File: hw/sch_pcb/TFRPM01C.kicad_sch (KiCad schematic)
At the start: 22 parts, among them J1 HEADER_1x03, J2 SM04B-GHS-TB, J3 SM04B-GHS-TB, M2 M3, U1 PCF8583, U2 SN74LVC1G14-Q1, U3 MIC5504-3.3YM5

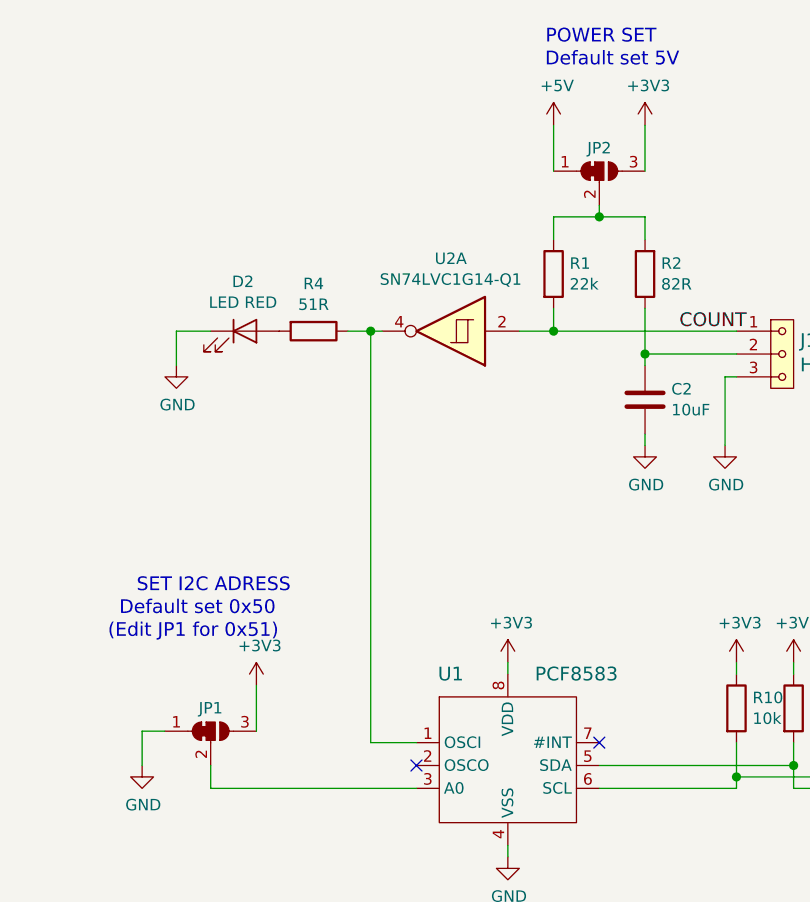
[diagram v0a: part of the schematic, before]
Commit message: update to newest kicad version, set schematic tempate, clean dps
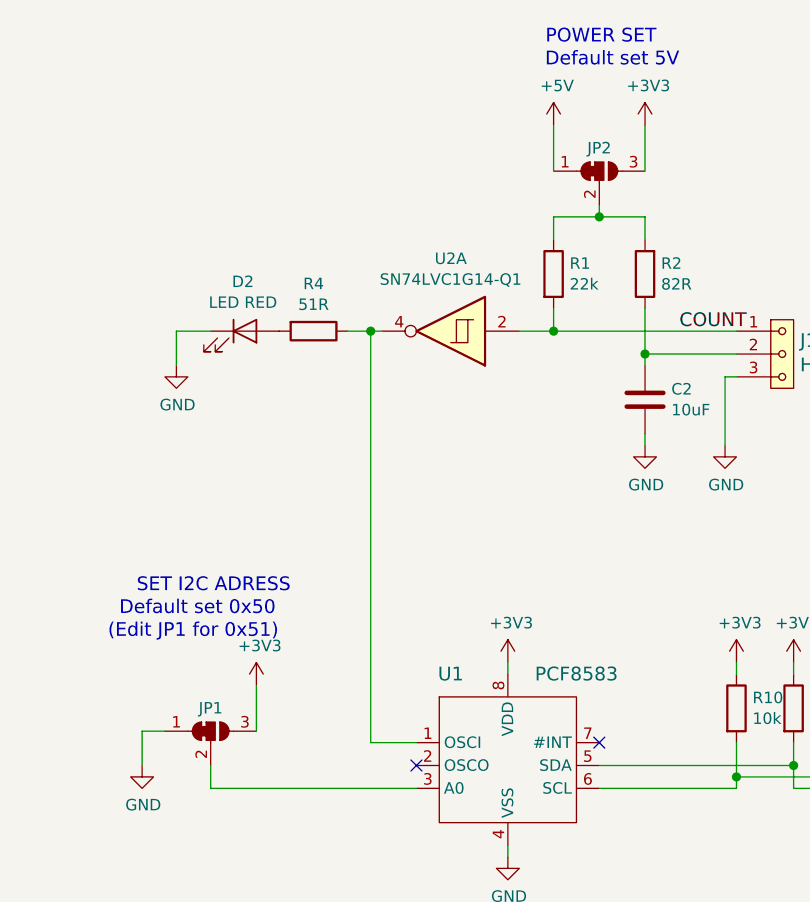
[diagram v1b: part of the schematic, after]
